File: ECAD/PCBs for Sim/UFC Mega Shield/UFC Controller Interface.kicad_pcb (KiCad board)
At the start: 2 copper layers, 101.6 x 53.3 mm, 13 parts, among them P1 Digital, P10 CONN_01X01, P11 CONN_01X01, P13 CONN_01X01, P14 MEGA CONN 2, P15 MEGA CONN 1, P2 Power, P3 Analog, P4 Analog, P5 PWM, P6 PWM, P7 Communication, P8 CONN_01X01

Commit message: Routed UFC Mega Shield
Routed UFC Mega Shield (#66)
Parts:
- moved P14 79.0 mm to (145.4, 90.2)
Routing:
- net GND: track 0.00 -> 118.3 mm, vias 0 -> 1
- net /A8: track 0.00 -> 78.6 mm
- net +5V: track 0.00 -> 74.2 mm
- net /A0: track 0.00 -> 71.5 mm
- net /A9: track 0.00 -> 70.2 mm
- net /A7: track 0.00 -> 64.0 mm, vias 0 -> 1
- net /A4: track 0.00 -> 62.3 mm, vias 0 -> 1
- net /A6: track 0.00 -> 61.1 mm, vias 0 -> 1
- net /53(SS): track 0.00 -> 59.7 mm
- net /52(SCK): track 0.00 -> 59.3 mm
- net /32: track 0.00 -> 59.3 mm
- net /A2: track 0.00 -> 58.6 mm
- net /Vin: track 0.00 -> 56.9 mm
- net /51(MOSI): track 0.00 -> 56.8 mm
- net /A5: track 0.00 -> 56.1 mm, vias 0 -> 1
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- added copper zone on B.Cu, net GND
- added copper zone on F.Cu, net GND

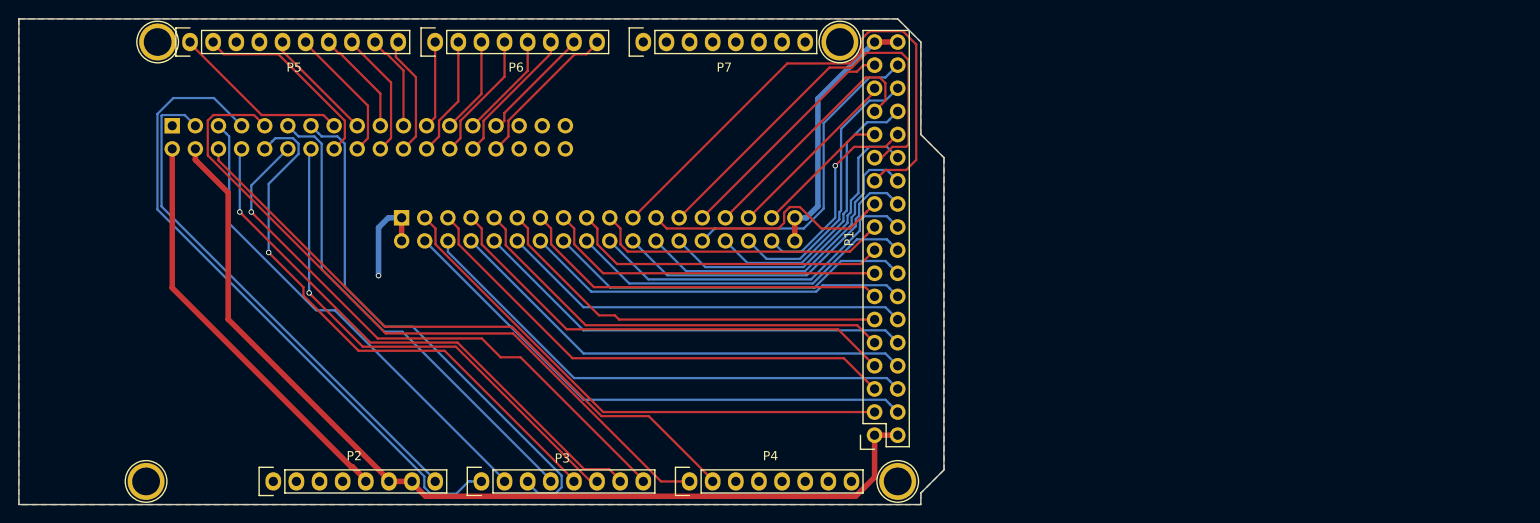
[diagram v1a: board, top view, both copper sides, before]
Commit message: rerouted UFC mega shield
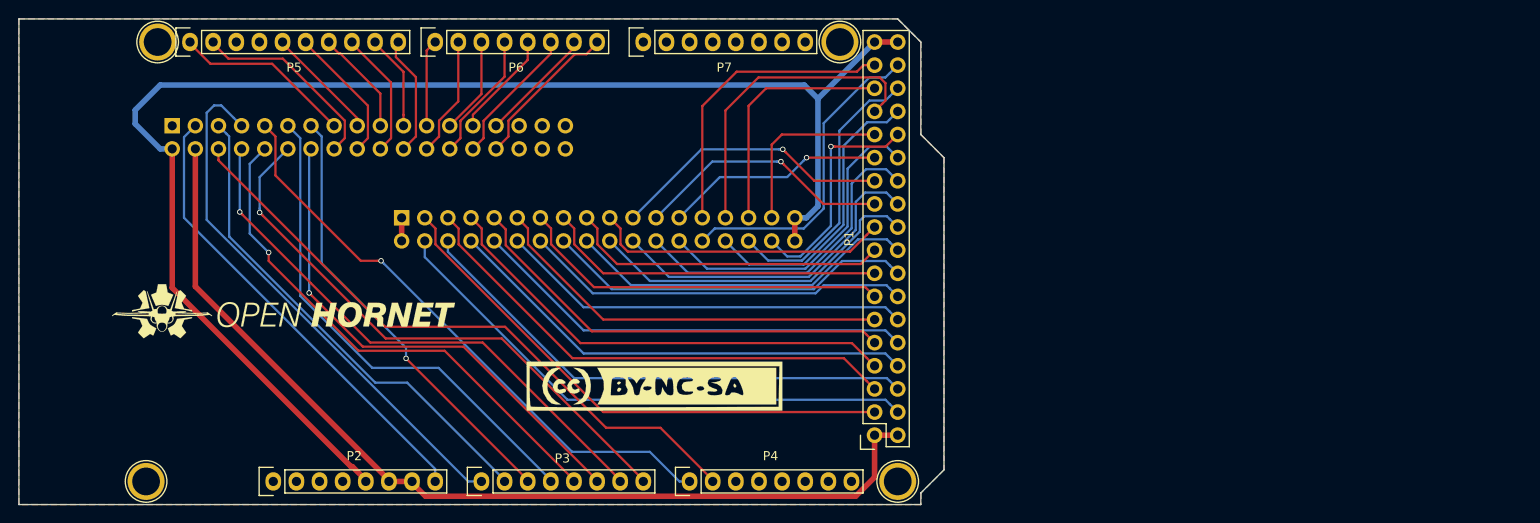
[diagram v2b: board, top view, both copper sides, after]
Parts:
- added G***: LOGO, KiCAD Libraries:CC-BY-NC-SA-Small, F.Cu at (173.1, 108.7)
- added G***: LOGO, KiCAD Libraries:OH_LOGO_37.7mm_5.9mm, F.Cu at (132.4, 100.4)
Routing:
- net +5V: track 74.2 -> 157.6 mm
- net /32: track 59.3 -> 31.1 mm, vias 0 -> 1
- net /30: track 46.6 -> 24.2 mm, vias 0 -> 1
- net /A8: track 78.6 -> 65.4 mm, vias 0 -> 1
- net /A0: track 71.5 -> 58.9 mm
- net /A2: track 58.6 -> 49.1 mm, vias 0 -> 1
- net GND: track 118.3 -> 110.0 mm, vias 1 -> 0
- net /22: track 25.9 -> 33.1 mm
- net /24: track 20.0 -> 26.9 mm
- net /26: track 27.8 -> 34.7 mm
- net /Vin: track 56.9 -> 51.0 mm
- net /A4: track 62.3 -> 57.5 mm
- net /28: track 15.1 -> 19.8 mm
- net /29: track 23.0 -> 25.2 mm
- net /A3: track 53.2 -> 55.3 mm
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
